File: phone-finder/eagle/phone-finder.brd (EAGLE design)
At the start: 52 parts, among them J1 MICRO USB, J2 SWD HEADER, K1 35701331, Q1 12Mhz, Q2 2N2222, Q3 2N2222, T1 DTA114EET1G (2x10K), U1 AP2114H-3.3TRG1, U2 NUF2042XV6T1G, U3 LPC11U35FHI33/501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

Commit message: Work in progress
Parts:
- Q2: device transistor-npn:SOT23-BEC -> transistor-npn:SOT23
- moved Q2 25.7 mm to (14.0, -40.1)
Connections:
- removed net N$21: Q2.E, R9.2
- new net N$8: Q2.2, R9.2
- net +5V: now also Q2.3; no longer Q2.C
- net N$23: now also Q2.1; no longer Q2.B
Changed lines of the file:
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@@
 <element name="R12" library="wifi-orb" package="R0402" value="100" x="12.7" y="-3.556"/>
 <element name="R9" library="wifi-orb" package="R0402" value="100" x="12.7" y="-8.382"/>
-<element name="Q2" library="transistor-npn" package="SOT23-BEC" value="2N2222" x="13.97" y="-14.478"/>
 <element name="C15" library="wifi-orb" package="C0603K" value="0.1uF" x="12.954" y="-20.32"/>
 <element name="R7" library="wifi-orb" package="R0402" value="3K" x="12.7" y="-24.892"/>
 <element name="R8" library="wifi-orb" package="R0402" value="3K" x="12.7" y="-29.718"/>
 <element name="C16" library="wifi-orb" package="C0603K" value="0.1uF" x="12.954" y="-34.29"/>
+<element name="Q2" library="transistor-npn" package="SOT23" value="2N2222" x="13.97" y="-40.132"/>
 </elements>
 <signals>
@@
 <contactref element="C5" pad="+"/>
 <contactref element="K1" pad="3"/>
-<contactref element="Q2" pad="C"/>
+<contactref element="Q2" pad="3"/>
 <wire x1="17.876" y1="75.931" x2="18.185" y2="80.226" width="0" layer="19" extent="1-1"/>
 <wire x1="15.629" y1="76.7" x2="17.876" y2="75.931" width="0" layer="19" extent="1-1"/>
@@
 <wire x1="27.456" y1="62.685" x2="20.8472" y2="63.2166" width="0" layer="19" extent="1-1"/>
 <wire x1="39.116" y1="52.07" x2="27.456" y2="62.685" width="0" layer="19" extent="1-1"/>
-<wire x1="13.97" y1="-13.378" x2="39.116" y2="52.07" width="0" layer="19" extent="1-1"/>
+<wire x1="13.97" y1="-39.032" x2="39.116" y2="52.07" width="0" layer="19" extent="1-1"/>
 </signal>
 <signal name="N$6">
@@
 <wire x1="12.15" y1="-8.382" x2="16.51" y2="51.054" width="0" layer="19" extent="1-1"/>
 </signal>
-<signal name="N$21">
-<contactref element="Q2" pad="E"/>
-<contactref element="R9" pad="2"/>
-<wire x1="14.92" y1="-15.578" x2="13.25" y2="-8.382" width="0" layer="19" extent="1-1"/>
-</signal>
 <signal name="N$23">
 <contactref element="C15" pad="1"/>
-<contactref element="Q2" pad="B"/>
 <contactref element="R7" pad="2"/>
 <contactref element="R8" pad="2"/>
+<contactref element="Q2" pad="1"/>
+<wire x1="13.25" y1="-29.718" x2="13.02" y2="-41.232" width="0" layer="19" extent="1-1"/>
 <wire x1="13.25" y1="-24.892" x2="13.25" y2="-29.718" width="0" layer="19" extent="1-1"/>
 <wire x1="12.079" y1="-20.32" x2="13.25" y2="-24.892" width="0" layer="19" extent="1-1"/>
-<wire x1="13.02" y1="-15.578" x2="12.079" y2="-20.32" width="0" layer="19" extent="1-1"/>
+</signal>
+<signal name="N$8">
+<contactref element="R9" pad="2"/>
+<contactref element="Q2" pad="2"/>
+<wire x1="13.25" y1="-8.382" x2="14.92" y2="-41.232" width="0" layer="19" extent="1-1"/>
 </signal>
 </signals>

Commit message: Associated schematic parts with library parts.
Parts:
- ANTENNA, LINE1, LINE2: device pinhead:1X01 -> phone-finder:1X01
- C1, C2: device wifi-orb:C0402K -> phone-finder:C0402K
- C10, C11, C13, C17, C3, C4: device wifi_orb:C0603K -> phone-finder:C0402K
- C12, C14, C9: device wifi_orb:C0805K -> phone-finder:C0805K
- C15, C16: device wifi-orb:C0603K -> phone-finder:C0402K
- C5, C8: device wifi-orb:UD-6,3X5,8_NICHICON -> phone-finder:UD-6,3X5,8_NICHICON
- C6, C7: device wifi_orb:C0603K -> phone-finder:C0603K
- D1: device diode:AG -> phone-finder:AG
- D2: device wifi_orb:SOT23 -> phone-finder:SOT23
- J1: device wifi_orb:USB-MICRO -> phone-finder:USB-MICRO
- J2: device wifi_orb:SWD-HEADER -> phone-finder:SWD-HEADER
- K1: value 35701331 -> RELAY; device relay:REED -> phone-finder:REED
- MH$1, MH$2, MH$3, MH$4: value MOUNTING_HOLE -> MOUNTING-HOLE; device wifi_orb:MOUNTING_HOLE -> phone-finder:MOUNTING_HOLE
- Q1: device wifi-orb:CRYSTAL -> phone-finder:CRYSTAL
- Q2, Q3: device transistor-npn:SOT23 -> phone-finder:SOT23
- R1, R2, R3, R4, R5, R6: device wifi_orb:R0402 -> phone-finder:R0402
- R10, R12, R9: device wifi-orb:R0402 -> phone-finder:R0805
- R11, R7, R8: device wifi-orb:R0402 -> phone-finder:R0402
- S1, S2: value PUSH_BUTTON -> PUSH-BUTTON; device wifi_orb:PUSH_BUTTON -> phone-finder:PUSH_BUTTON
- T1: device wifi_orb:SC75-BEC -> phone-finder:SC75-BEC
- TR1: value PE-65612 -> TRANSFORMER; device transformer-pulse:PE-65612 -> phone-finder:PE-65612
- U1: device wifi-orb:SOT223 -> phone-finder:SOT223
- U2: device wifi-orb:SOT-563 -> phone-finder:SOT-563
- U3: device wifi_orb:HVQFN33-5MM -> phone-finder:HVQFN33-5MM
- U4: device wifi_orb:WIFI_MODULE -> phone-finder:WIFI_MODULE

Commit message: Work in progress.
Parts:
- removed LINE1, LINE2: (no value), phone-finder:1X01
- added D3: SFH482, led:SFH482
- added J3: SWD HEADER, phone-finder:SWD-HEADER
- added R13: 1K5, phone-finder:R0402
- ANTENNA: device phone-finder:1X01 -> phone-finder:PINHD-1X1
- D1: device phone-finder:AG -> phone-finder:DZ-0402
- J2: value SWD HEADER -> PHONE-JACK; device phone-finder:SWD-HEADER -> phone-finder:PHONE-JACK
- moved MH$3 115.4 mm to (3.00, 3.00)
- moved MH$4 90.9 mm to (3.00, 47.0)
- moved MH$2 76.9 mm to (47.0, 3.00)
- moved Q2 67.5 mm to (38.4, 22.9)
- moved R8 64.6 mm to (16.5, 34.8), turned to 90 degrees
- moved J2 62.3 mm to (10.4, 12.4), turned to 270 degrees
- moved R10 59.8 mm to (43.9, 11.2)
- moved C16 58.0 mm to (40.9, 16.5), turned to 180 degrees
- moved MH$1 57.3 mm to (47.0, 47.0)
- moved K1 54.4 mm to (28.2, 0.51)
- moved D2 52.1 mm to (24.5, 14.2)
- moved TR1 50.9 mm to (36.3, 4.83)
- moved R7 50.9 mm to (43.7, 15.5)
- moved Q3 50.2 mm to (31.8, 13.7)
- moved C6 48.1 mm to (8.07, 19.6), turned to 180 degrees
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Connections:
- removed net N$9 (its old number): K1.7, LINE1.1
- new net LED: R13.1, U3.7
- new net N$11: J2.2, K1.7
- new net N$14: D3.A, R13.2
- net +3V3: now also J3.1; no longer J2.1
- net GND: now also D3.K, J3.3, J3.5, J3.7, J3.9; no longer J2.3, J2.5, J2.7, J2.9
- net N$10: now also D1.1, J2.3; no longer D1.A, LINE2.1
- net N$15: now also D1.2; no longer D1.C
- net RESET: now also J3.10; no longer J2.10
- net SWDCLK: now also J3.4; no longer J2.4
- net SWDIO: now also J3.2; no longer J2.2
- net SWDO: now also J3.6; no longer J2.6
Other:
- board outline added: 50 x 50 mm

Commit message: Worked in progress. Cleanedup some of the library components.
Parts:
- K1: device phone-finder:REED -> phone-finder:RELAY
- TR1: device phone-finder:PE-65612 -> phone-finder:TRANSFORMER
- moved D2 47.3 mm to (63.6, 40.8)
- moved D3 37.5 mm to (64.3, 33.0)
- moved R9 32.5 mm to (67.1, 25.7)
- moved Q2 21.0 mm to (58.9, 26.9)
- moved R10 20.7 mm to (23.6, 7.11), turned to 180 degrees
- moved C16 16.6 mm to (26.9, 7.62), turned to 90 degrees
- moved D1 16.0 mm to (23.4, 9.91), turned to 180 degrees
- moved C15 12.0 mm to (57.4, 6.86)
- moved K1 11.2 mm to (17.3, 3.05)
- moved Q3 9.66 mm to (22.1, 13.5), turned to 180 degrees
- moved R11 8.52 mm to (25.1, 14.5), turned to 90 degrees
- moved R12 5.34 mm to (19.8, 9.14), turned to 270 degrees
- moved TR1 3.75 mm to (34.5, 8.13), turned to 180 degrees
- moved C8 3.45 mm to (22.6, 20.4)
- moved R4 2.81 mm to (7.56, 26.3)
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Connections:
- net +5V: now also K1.2; no longer K1.3
- net GND: now also TR1.6; no longer TR1.2
- net N$10: now also TR1.1; no longer TR1.4
- net N$11: now also J2.4, K1.1; no longer J2.2, K1.7
- net N$17: now also TR1.4; no longer TR1.1
- net N$20: now also K1.4; no longer K1.1
- net N$4: now also K1.3; no longer K1.5

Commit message: Work in progress.
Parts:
- D3: value SFH482 -> LED; device led:SFH482 -> phone-finder:LED
- moved D3 35.7 mm to (31.8, 18.3)
- moved R9 30.4 mm to (37.6, 18.0), turned to 0 degrees
- moved C12 30.2 mm to (20.0, 34.6), turned to 270 degrees
- moved D2 30.1 mm to (40.7, 21.3)
- moved C15 29.2 mm to (32.0, 21.3), turned to 180 degrees
- moved C14 28.9 mm to (47.4, 41.5), turned to 90 degrees
- moved C17 24.4 mm to (14.8, 44.9), turned to 180 degrees
- moved Q2 23.4 mm to (36.1, 21.8), turned to 90 degrees
- moved R8 18.4 mm to (30.5, 22.9), turned to 0 degrees
- moved C7 16.6 mm to (16.9, 21.1), turned to 0 degrees
- moved R7 13.0 mm to (33.0, 22.9)
- moved R3 10.9 mm to (15.0, 43.6), turned to 0 degrees
- moved C11 9.43 mm to (21.4, 33.5)
- moved R4 7.55 mm to (1.98, 31.4)
- moved J3 5.59 mm to (7.42, 31.1)
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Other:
- board text added: "PRG"
- board text added: "RUN"
- board text removed: "ISP"
- board text removed: "RST"

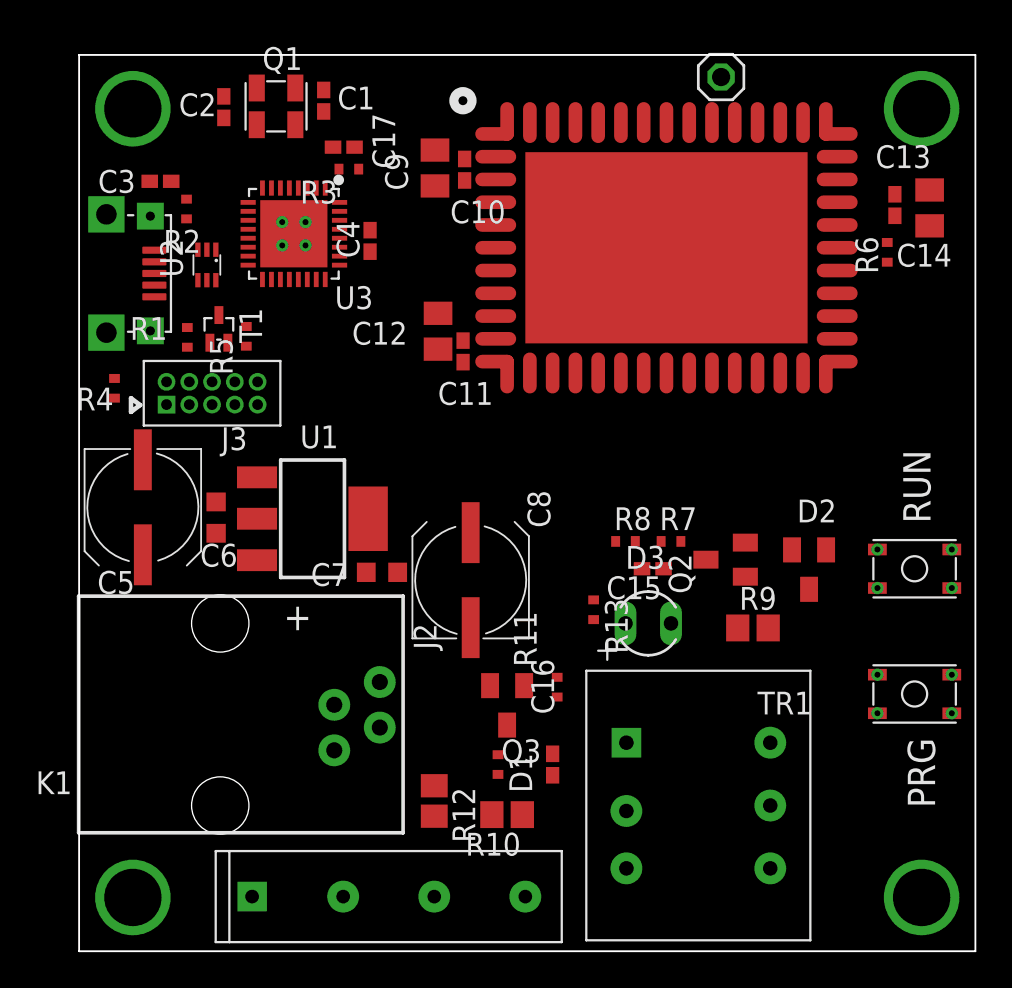
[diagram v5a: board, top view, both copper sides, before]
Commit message: Removed the mounting holes. Stable placement.
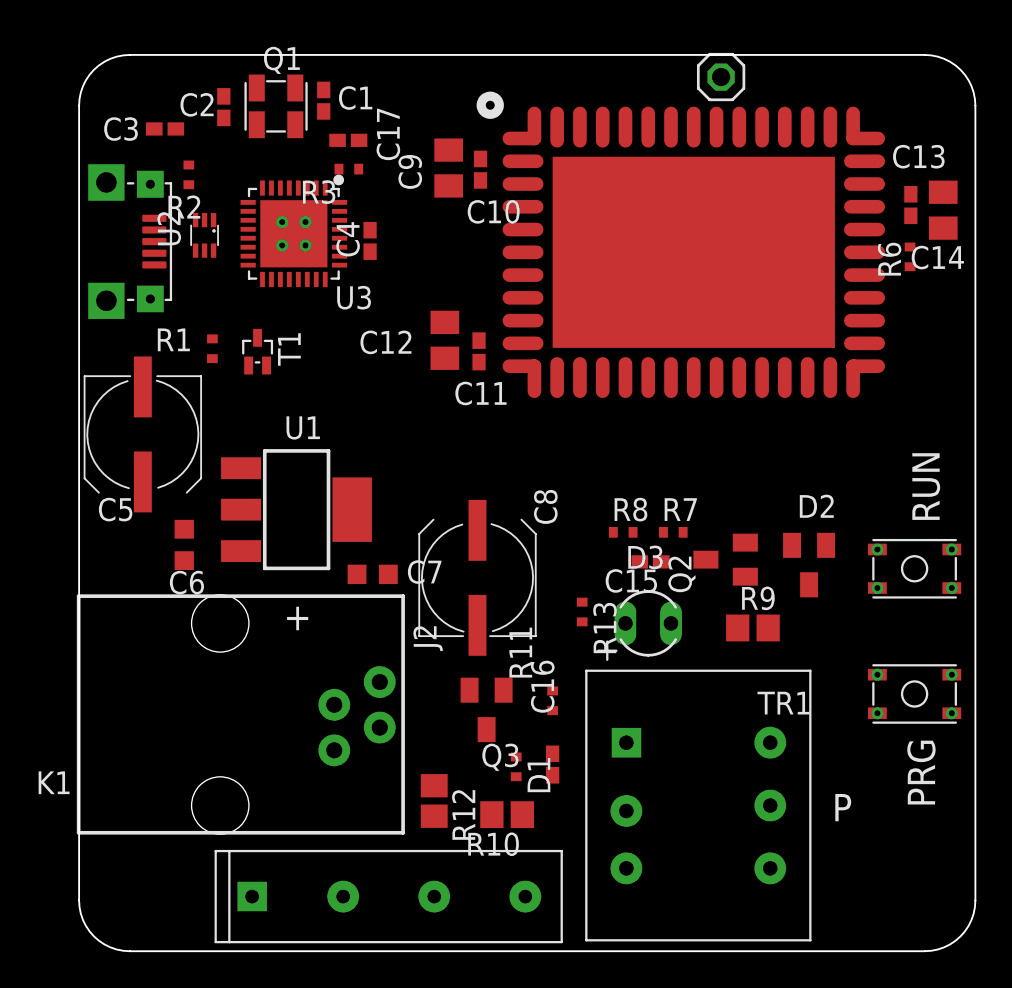
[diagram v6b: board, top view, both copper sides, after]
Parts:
- removed J3: SWD HEADER, phone-finder:SWD-HEADER
- removed MH$1, MH$2, MH$3, MH$4: MOUNTING-HOLE, phone-finder:MOUNTING_HOLE
- removed R4, R5: 10K, phone-finder:R0402
- moved C5 4.06 mm to (3.56, 28.8)
- moved C3 2.93 mm to (4.79, 45.9)
- moved T1 2.50 mm to (9.96, 33.4)
- moved C6 2.34 mm to (5.87, 22.7)
- moved R2 1.91 mm to (6.12, 43.3)
- moved J1 1.78 mm to (1.52, 39.6)
- moved U2 1.66 mm to (7.00, 39.9)
- moved U4 1.55 mm to (24.1, 31.4)
- moved R1 1.53 mm to (7.44, 33.6)
- moved R6 1.30 mm to (46.4, 38.7)
- moved Q3 1.17 mm to (22.7, 13.5)
- moved D1 1.02 mm to (24.4, 10.3)
- moved U1 1.02 mm to (12.1, 24.6)
- moved C13 0.89 mm to (46.4, 41.6)
- moved C10 0.89 mm to (22.4, 43.6)
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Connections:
- removed net SWDCLK: J3.4, R5.2, U3.19
- removed net SWDIO: J3.2, R4.1, U3.25
- removed net SWDO: J3.6, U3.18
- net +3V3: no longer J3.1, R4.2
- net GND: no longer J3.3, J3.5, J3.7, J3.9, R5.1
- net RESET: no longer J3.10
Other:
- outline, holes or cut-outs redrawn
- board text added: "P"
